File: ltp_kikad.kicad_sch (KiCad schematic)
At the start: 27 parts, among them J2 RPi_GPIO, J3 SM04B-SRSS-TB(LF)(SN)

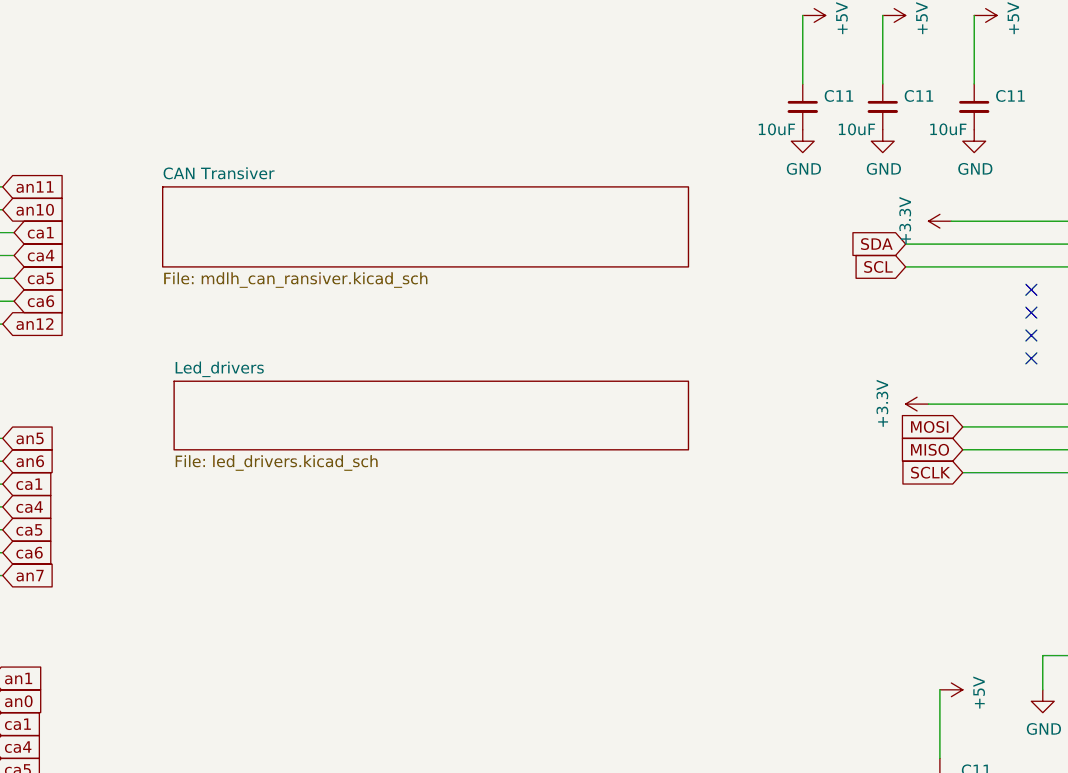
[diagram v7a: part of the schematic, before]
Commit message: Add PCA9306 i2c transciever
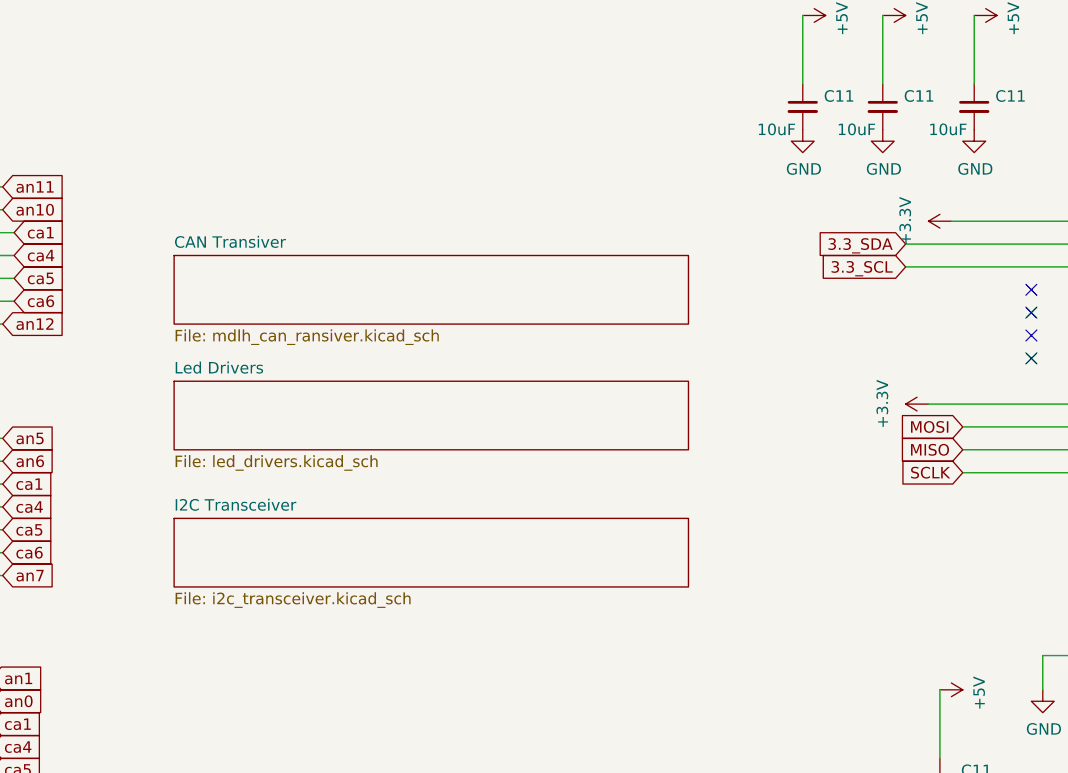
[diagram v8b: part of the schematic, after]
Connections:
- net SCL: no longer J2.5 (BCM3_SCL)
- net SDA: no longer J2.3 (BCM2_SDA)
- new net 3.3_SCL: J2.5 (BCM3_SCL)
- new net 3.3_SDA: J2.3 (BCM2_SDA)
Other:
- sheet Led_drivers renamed Led Drivers
- added sheet I2C Transceiver (i2c_transceiver.kicad_sch)
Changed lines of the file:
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@@
     )
   )
-  (global_label "SCL" (shape input) (at 198.12 46.99 180)
+  (global_label "3.3_SCL" (shape input) (at 198.12 46.99 180)
     (effects (font (size 1.27 1.27)) (justify right))
     (property "Intersheetrefs" "${INTERSHEET_REFS}" (at 191.7066 46.99 0)
@@
     )
   )
-  (global_label "SDA" (shape input) (at 198.12 44.45 180)
+  (global_label "3.3_SDA" (shape input) (at 198.12 44.45 180)
     (effects (font (size 1.27 1.27)) (justify right))
     (property "Intersheetrefs" "${INTERSHEET_REFS}" (at 198.12 44.45 0)
@@
     )
   )
+  (sheet (at 116.84 74.93) (size 57.15 7.62) (fields_autoplaced)
+    (stroke (width 0.1524) (type solid))
+    (fill (color 0 0 0 0.0000))
+    (property "Sheetname" "I2C Transceiver" (at 116.84 74.2184 0)
+      (effects (font (size 1.27 1.27)) (justify left bottom))
+    )
+    (property "Sheetfile" "i2c_transceiver.kicad_sch" (at 116.84 83.1346 0)
+      (effects (font (size 1.27 1.27)) (justify left top))
+    )
+    (instances
+      (project "ltp_kikad"
+        (path "/eed35b77-cbf9-4596-9b17-2558f81058ba" (page "4"))
+      )
+    )
+  )
   (sheet (at 116.84 59.69) (size 57.15 7.62) (fields_autoplaced)
     (stroke (width 0.1524) (type solid))
     (fill (color 0 0 0 0.0000))
-    (property "Sheetname" "Led_drivers" (at 116.84 58.9784 0)
+    (property "Sheetname" "Led Drivers" (at 116.84 58.9784 0)
       (effects (font (size 1.27 1.27)) (justify left bottom))
     )
@@
     )
   )
-  (sheet (at 115.57 38.1) (size 58.42 8.89) (fields_autoplaced)
+  (sheet (at 116.84 45.72) (size 57.15 7.62) (fields_autoplaced)
     (stroke (width 0.1524) (type solid))
     (fill (color 0 0 0 0.0000))
-    (property "Sheetname" "CAN Transiver" (at 115.57 37.3884 0)
+    (property "Sheetname" "CAN Transiver" (at 116.84 45.0084 0)
       (effects (font (size 1.27 1.27)) (justify left bottom))
     )
-    (property "Sheetfile" "mdlh_can_ransiver.kicad_sch" (at 115.57 47.5746 0)
+    (property "Sheetfile" "mdlh_can_ransiver.kicad_sch" (at 116.84 53.9246 0)
       (effects (font (size 1.27 1.27)) (justify left top))
     )
